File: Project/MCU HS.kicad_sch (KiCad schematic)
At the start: 21 parts, among them J2 SM04B, U1 STM32F072CBUx, U3 XC6206PxxxMR, U4 PRTR5V0U2X

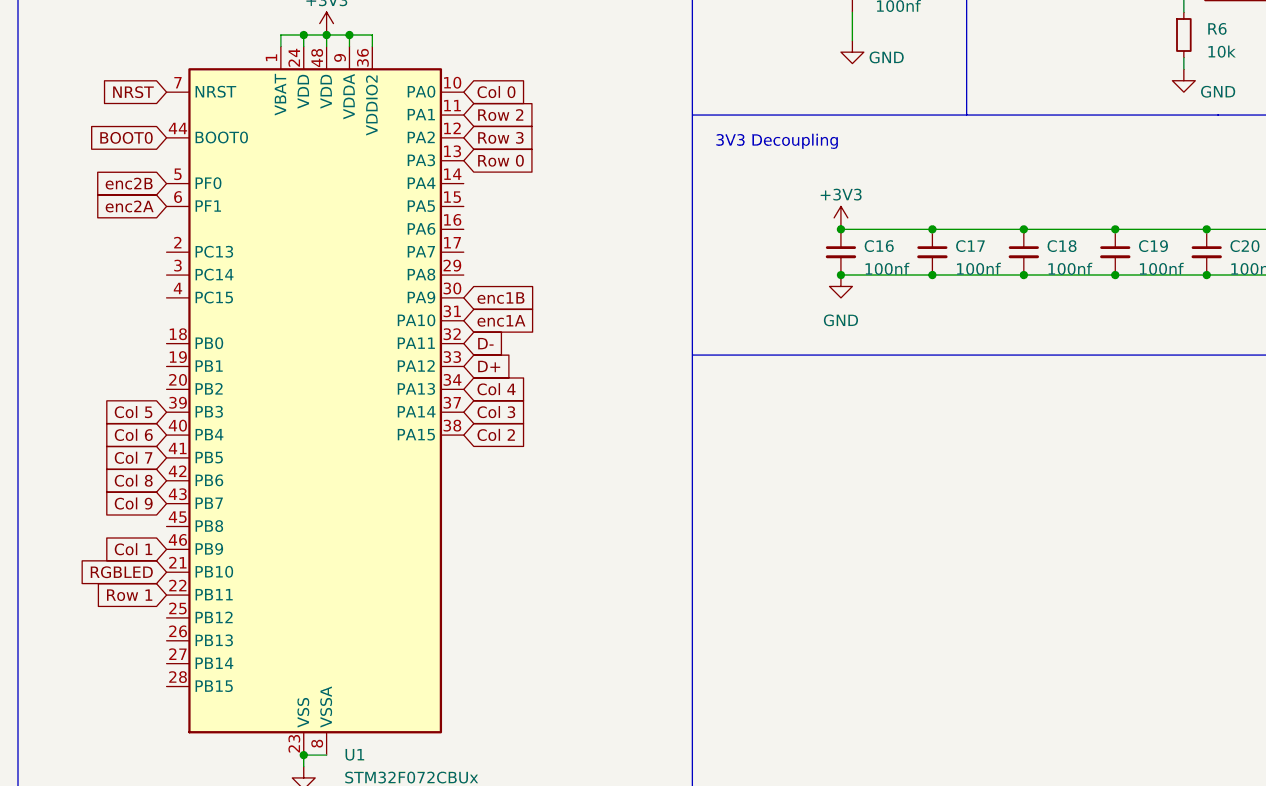
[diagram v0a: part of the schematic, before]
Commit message: 6 MCU pin breakouts added, readded silkscreen, fresh production files
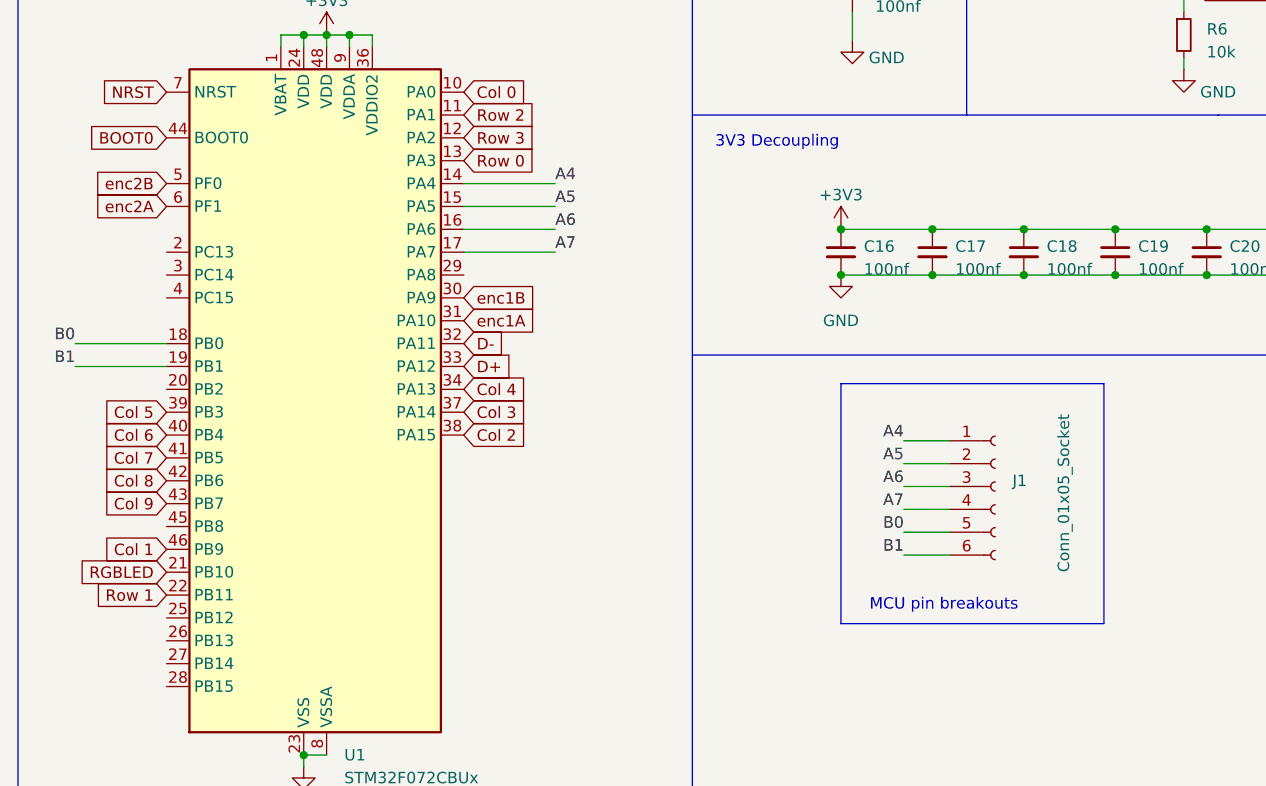
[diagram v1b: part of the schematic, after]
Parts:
- added J1: Conn_01x05_Socket, Connector_PinHeader_2.00mm:PinHeader_1x06_P2.00mm_Vertical, symbol Connector:Conn_01x06_Socket
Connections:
- net A4: now reaches U1.14 (PA4)
- net A4: now also J1.1 (Pin_1)
- net A5: now reaches U1.15 (PA5)
- net A5: now also J1.2 (Pin_2)
- net A6: now reaches U1.16 (PA6)
- net A6: now also J1.3 (Pin_3)
- net A7: now reaches U1.17 (PA7)
- net A7: now also J1.4 (Pin_4)
- net B0: now reaches U1.18 (PB0)
- net B0: now also J1.5 (Pin_5)
- net B1: now reaches U1.19 (PB1)
- net B1: now also J1.6 (Pin_6)
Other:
- note added: "MCU pin breakouts"
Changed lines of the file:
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@@
+    (stroke (width 0) (type default))
+  )
+  (wire (pts (xy 68.58 49.53) (xy 78.74 49.53))
     (stroke (width 0) (type default))
   )
@@
     (stroke (width 0) (type default))
   )
+  (wire (pts (xy 117.475 85.725) (xy 122.555 85.725))
+    (stroke (width 0) (type default))
+  )
   (wire (pts (xy 50.8 113.03) (xy 53.34 113.03))
     (stroke (width 0) (type default))
@@
     (stroke (width 0) (type default))
   )
+  (wire (pts (xy 117.475 78.105) (xy 122.555 78.105))
+    (stroke (width 0) (type default))
+  )
   (wire (pts (xy 262.89 52.07) (xy 264.795 52.07))
     (stroke (width 0) (type default))
@@
     (stroke (width 0) (type default))
   )
+  (wire (pts (xy 117.475 90.805) (xy 122.555 90.805))
+    (stroke (width 0) (type default))
+  )
   (polyline (pts (xy 93.98 68.58) (xy 171.45 68.58))
     (stroke (width 0) (type default))
@@
     (stroke (width 0) (type default))
   )
+  (wire (pts (xy 35.56 67.31) (xy 25.4 67.31))
+    (stroke (width 0) (type default))
+  )
   (wire (pts (xy 148.59 27.94) (xy 148.59 30.48))
     (stroke (width 0) (type default))
@@
     (stroke (width 0) (type default))
   )
+  (wire (pts (xy 68.58 57.15) (xy 78.74 57.15))
+    (stroke (width 0) (type default))
+  )
   (wire (pts (xy 224.155 76.835) (xy 224.155 84.455))
     (stroke (width 0) (type default))
@@
     (stroke (width 0) (type default))
   )
+  (wire (pts (xy 117.475 88.265) (xy 122.555 88.265))
+    (stroke (width 0) (type default))
+  )
   (wire (pts (xy 231.14 31.75) (xy 240.665 31.75))
     (stroke (width 0) (type default))
@@
     (stroke (width 0) (type default))
   )
+  (wire (pts (xy 68.58 52.07) (xy 78.74 52.07))
+    (stroke (width 0) (type default))
+  )
+  (wire (pts (xy 68.58 54.61) (xy 78.74 54.61))
+    (stroke (width 0) (type default))
+  )
   (polyline (pts (xy 278.13 66.04) (xy 208.28 66.04))
     (stroke (width 0) (type default))
@@
     (stroke (width 0) (type default))
   )
+  (wire (pts (xy 35.56 69.85) (xy 25.4 69.85))
+    (stroke (width 0) (type default))
+  )
   (wire (pts (xy 270.51 78.74) (xy 270.51 80.645))
     (stroke (width 0) (type default))
   )
+  (wire (pts (xy 117.475 80.645) (xy 122.555 80.645))
+    (stroke (width 0) (type default))
+  )
+  (wire (pts (xy 117.475 83.185) (xy 122.555 83.185))
+    (stroke (width 0) (type default))
+  )
   (wire (pts (xy 226.695 101.6) (xy 234.95 101.6))
     (stroke (width 0) (type default))
@@
     (stroke (width 0) (type default))
   )
+  (rectangle (start 110.49 71.755) (end 139.7 98.425)
+    (stroke (width 0) (type default))
+    (fill (type none))
+  )
   (text "Power Regulation" (at 209.55 95.25 0)
     (effects (font (size 1.27 1.27)) (justify left bottom))
@@
   )
   (text "3V3 Decoupling" (at 96.52 45.72 0)
+    (effects (font (size 1.27 1.27)) (justify left bottom))
+  )
+  (text "MCU pin breakouts" (at 113.665 97.155 0)
+    (effects (font (size 1.27 1.27)) (justify left bottom))
+  )
+  (label "A4" (at 117.475 78.105 180) (fields_autoplaced)
+    (effects (font (size 1.27 1.27)) (justify right bottom))
+  )
+  (label "A7" (at 117.475 85.725 180) (fields_autoplaced)
+    (effects (font (size 1.27 1.27)) (justify right bottom))
+  )
+  (label "B1" (at 117.475 90.805 180) (fields_autoplaced)
+    (effects (font (size 1.27 1.27)) (justify right bottom))
+  )
+  (label "A6" (at 117.475 83.185 180) (fields_autoplaced)
+    (effects (font (size 1.27 1.27)) (justify right bottom))
+  )
+  (label "B0" (at 25.4 67.31 180) (fields_autoplaced)
+    (effects (font (size 1.27 1.27)) (justify right bottom))
+  )
+  (label "A6" (at 78.74 54.61 0) (fields_autoplaced)
+    (effects (font (size 1.27 1.27)) (justify left bottom))
+  )
+  (label "B0" (at 117.475 88.265 180) (fields_autoplaced)
+    (effects (font (size 1.27 1.27)) (justify right bottom))
+  )
+  (label "A4" (at 78.74 49.53 0) (fields_autoplaced)
+    (effects (font (size 1.27 1.27)) (justify left bottom))
+  )
+  (label "B1" (at 25.4 69.85 180) (fields_autoplaced)
+    (effects (font (size 1.27 1.27)) (justify right bottom))
+  )
+  (label "A7" (at 78.74 57.15 0) (fields_autoplaced)
+    (effects (font (size 1.27 1.27)) (justify left bottom))
+  )
+  (label "A5" (at 117.475 80.645 180) (fields_autoplaced)
+    (effects (font (size 1.27 1.27)) (justify right bottom))
+  )
+  (label "A5" (at 78.74 52.07 0) (fields_autoplaced)
     (effects (font (size 1.27 1.27)) (justify left bottom))
   )
@@
         )
       )
+    )
+  )
+  (symbol (lib_id "Connector:Conn_01x06_Socket") (at 127.635 83.185 0) (unit 1)
+    (in_bom yes) (on_board yes) (dnp no)
+    (property "Reference" "J1" (at 129.54 82.55 0)
+      (effects (font (size 1.27 1.27)) (justify left))
+    )
+    (property "Value" "Conn_01x05_Socket" (at 135.255 92.71 90)
+      (effects (font (size 1.27 1.27)) (justify left))
+    )
+    (property "Footprint" "Connector_PinHeader_2.00mm:PinHeader_1x06_P2.00mm_Vertical" (at 127.635 83.185 0)
+      (effects (font (size 1.27 1.27)) hide)
+    )
+    (property "Datasheet" "~" (at 127.635 83.185 0)
+      (effects (font (size 1.27 1.27)) hide)
+    )
+    (pin "1")
+    (pin "2")
+    (pin "3")
+    (pin "4")
+    (pin "5")
+    (pin "6")
+    (instances
+      (project "Infernum HS"
+        (path "/e63e39d7-6ac0-4ffd-8aa3-1841a4541b55/d0969589-facd-430d-a52b-74c4e073ccb0"
+          (reference "J1") (unit 1)
+        )
+      )

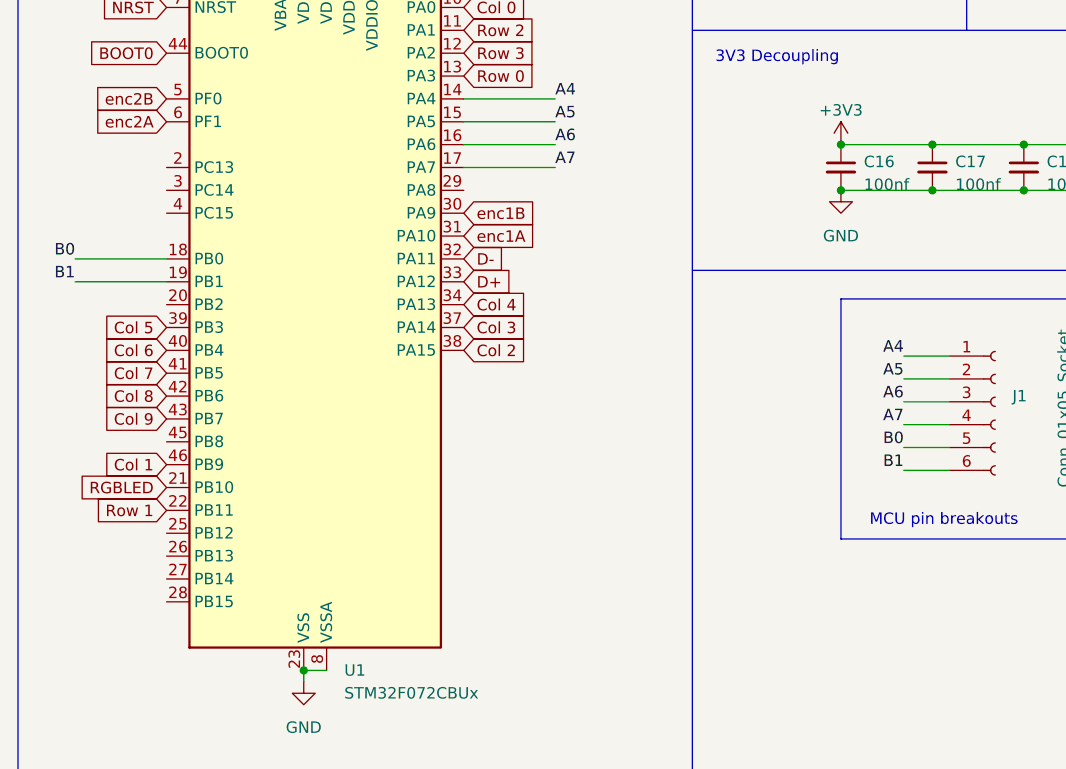
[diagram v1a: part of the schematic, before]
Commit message: changed pinout for pimoroni support, fresh gerbers
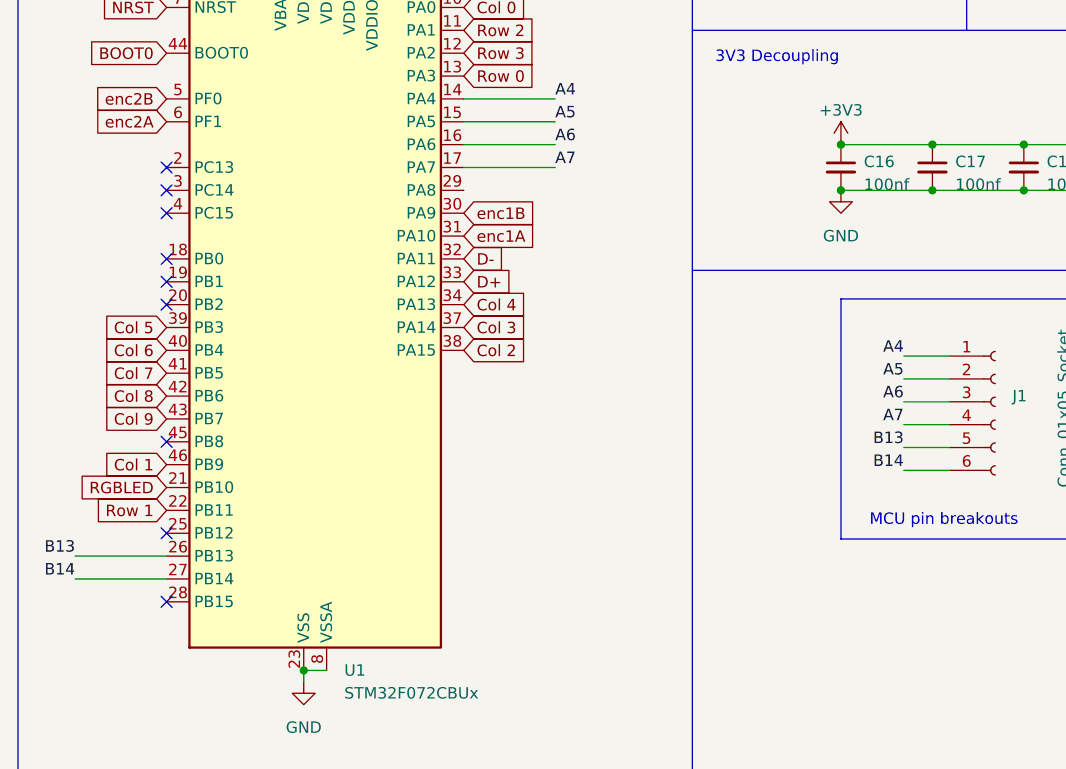
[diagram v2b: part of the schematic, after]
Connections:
- net B13: now reaches U1.26 (PB13)
- net B13: now also J1.5 (Pin_5)
- net B14: now reaches U1.27 (PB14)
- net B14: now also J1.6 (Pin_6)
- net B0: no longer names the net of U1.18 (PB0)
- net B0: no longer J1.5 (Pin_5)
- net B1: no longer names the net of U1.19 (PB1)
- net B1: no longer J1.6 (Pin_6)
- no-connect marks 2 -> 11
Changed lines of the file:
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@@
   (junction (at 140.97 59.69) (diameter 0) (color 0 0 0 0)
   )
+  (no_connect (at 35.56 87.63))
+  (no_connect (at 35.56 67.31))
+  (no_connect (at 35.56 105.41))
+  (no_connect (at 35.56 69.85))
+  (no_connect (at 35.56 72.39))
   (no_connect (at 231.14 34.29))
+  (no_connect (at 35.56 62.23))
+  (no_connect (at 35.56 97.79))
+  (no_connect (at 35.56 57.15))
   (no_connect (at 231.14 49.53))
+  (no_connect (at 35.56 59.69))
   (wire (pts (xy 50.8 114.3) (xy 50.8 113.03))
     (stroke (width 0) (type default))
@@
     (stroke (width 0) (type default))
   )
-  (wire (pts (xy 35.56 67.31) (xy 25.4 67.31))
-    (stroke (width 0) (type default))
-  )
   (wire (pts (xy 148.59 27.94) (xy 148.59 30.48))
     (stroke (width 0) (type default))
@@
     (stroke (width 0) (type default))
   )
+  (wire (pts (xy 35.56 102.87) (xy 25.4 102.87))
+    (stroke (width 0) (type default))
+  )
+  (wire (pts (xy 35.56 100.33) (xy 25.4 100.33))
+    (stroke (width 0) (type default))
+  )
   (wire (pts (xy 68.58 54.61) (xy 78.74 54.61))
     (stroke (width 0) (type default))
@@
     (stroke (width 0) (type default))
   )
-  (wire (pts (xy 35.56 69.85) (xy 25.4 69.85))
-    (stroke (width 0) (type default))
-  )
   (wire (pts (xy 270.51 78.74) (xy 270.51 80.645))
     (stroke (width 0) (type default))
@@
     (effects (font (size 1.27 1.27)) (justify right bottom))
   )
-  (label "B1" (at 117.475 90.805 180) (fields_autoplaced)
+  (label "B14" (at 117.475 90.805 180) (fields_autoplaced)
+    (effects (font (size 1.27 1.27)) (justify right bottom))
+  )
+  (label "B13" (at 25.4 100.33 180) (fields_autoplaced)
     (effects (font (size 1.27 1.27)) (justify right bottom))
   )
@@
     (effects (font (size 1.27 1.27)) (justify right bottom))
   )
-  (label "B0" (at 25.4 67.31 180) (fields_autoplaced)
+  (label "B14" (at 25.4 102.87 180) (fields_autoplaced)
     (effects (font (size 1.27 1.27)) (justify right bottom))
   )
@@
     (effects (font (size 1.27 1.27)) (justify left bottom))
   )
-  (label "B0" (at 117.475 88.265 180) (fields_autoplaced)
+  (label "B13" (at 117.475 88.265 180) (fields_autoplaced)
     (effects (font (size 1.27 1.27)) (justify right bottom))
   )
@@
     (effects (font (size 1.27 1.27)) (justify left bottom))
   )
-  (label "B1" (at 25.4 69.85 180) (fields_autoplaced)
-    (effects (font (size 1.27 1.27)) (justify right bottom))
-  )
   (label "A7" (at 78.74 57.15 0) (fields_autoplaced)

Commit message: fresh production
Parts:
- added J4: Conn_01x03_Socket, Connector_PinHeader_2.00mm:PinHeader_1x03_P2.00mm_Vertical, symbol Connector:Conn_01x03_Socket
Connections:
- net +3V3: now also J4.2 (Pin_2)
- net +5V: now also J4.3 (Pin_3)
- net GND: now also J4.1 (Pin_1)
- no-connect marks 11 -> 12
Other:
- note added: "Power Breakout"
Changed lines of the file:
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@@
   (no_connect (at 35.56 57.15))
   (no_connect (at 231.14 49.53))
+  (no_connect (at 68.58 59.69))
   (no_connect (at 35.56 59.69))
   (wire (pts (xy 50.8 114.3) (xy 50.8 113.03))
@@
     (stroke (width 0) (type default))
   )
+  (rectangle (start 144.145 71.755) (end 170.815 98.425)
+    (stroke (width 0) (type default))
+    (fill (type none))
+  )
   (rectangle (start 110.49 71.755) (end 139.7 98.425)
     (stroke (width 0) (type default))
@@
   )
   (text "3V3 Decoupling" (at 96.52 45.72 0)
+    (effects (font (size 1.27 1.27)) (justify left bottom))
+  )
+  (text "Power Breakout" (at 144.78 97.155 0)
     (effects (font (size 1.27 1.27)) (justify left bottom))
   )
@@
     )
   )
+  (symbol (lib_id "power:GND") (at 153.035 82.55 270) (unit 1)
+    (in_bom yes) (on_board yes) (dnp no)
+    (property "Reference" "#PWR010" (at 146.685 82.55 0)
+      (effects (font (size 1.27 1.27)) hide)
+    )
+    (property "Value" "GND" (at 149.225 82.55 90)
+      (effects (font (size 1.27 1.27)) (justify right))
+    )
+    (property "Footprint" "" (at 153.035 82.55 0)
+      (effects (font (size 1.27 1.27)) hide)
+    )
+    (property "Datasheet" "" (at 153.035 82.55 0)
+      (effects (font (size 1.27 1.27)) hide)
+    )
+    (pin "1")
+    (instances
+      (project "Infernum HS"
+        (path "/e63e39d7-6ac0-4ffd-8aa3-1841a4541b55/d0969589-facd-430d-a52b-74c4e073ccb0"
+          (reference "#PWR010") (unit 1)
+        )
+      )
+    )
+  )
   (symbol (lib_id "Device:C_Small") (at 226.695 105.41 0) (unit 1)
     (in_bom yes) (on_board yes) (dnp no) (fields_autoplaced)
@@
         (path "/e63e39d7-6ac0-4ffd-8aa3-1841a4541b55/d0969589-facd-430d-a52b-74c4e073ccb0"
           (reference "C_LDO2") (unit 1)
+        )
+      )
+    )
+  )
+  (symbol (lib_id "power:+3V3") (at 153.035 85.09 90) (mirror x) (unit 1)
+    (in_bom yes) (on_board yes) (dnp no)
+    (property "Reference" "#PWR010" (at 156.845 85.09 0)
+      (effects (font (size 1.27 1.27)) hide)
+    )
+    (property "Value" "+3V3" (at 147.32 85.09 90)
+      (effects (font (size 1.27 1.27)))
+    )
+    (property "Footprint" "" (at 153.035 85.09 0)
+      (effects (font (size 1.27 1.27)) hide)
+    )
+    (property "Datasheet" "" (at 153.035 85.09 0)
+      (effects (font (size 1.27 1.27)) hide)
+    )
+    (pin "1")
+    (instances
+      (project "Eightu"
+        (path "/c4a24fcb-fcfe-47af-9a3c-3ffe86a38756"
+          (reference "#PWR010") (unit 1)
+        )
+      )
+      (project "stm32_hotswap_chiffre"
+        (path "/ca0d59d2-7f9b-4344-99bc-39bc2c8c88cb"
+          (reference "#PWR09") (unit 1)
+        )
+      )
+      (project "Infernum HS"
+        (path "/e63e39d7-6ac0-4ffd-8aa3-1841a4541b55/d0969589-facd-430d-a52b-74c4e073ccb0"
+          (reference "#PWR06") (unit 1)
         )
       )
@@
     )
   )
+  (symbol (lib_id "Connector:Conn_01x03_Socket") (at 158.115 85.09 0) (unit 1)
+    (in_bom yes) (on_board yes) (dnp no)
+    (property "Reference" "J4" (at 159.385 84.455 0)
+      (effects (font (size 1.27 1.27)) (justify left))
+    )
+    (property "Value" "Conn_01x03_Socket" (at 165.735 93.98 90)
+      (effects (font (size 1.27 1.27)) (justify left))
+    )
+    (property "Footprint" "Connector_PinHeader_2.00mm:PinHeader_1x03_P2.00mm_Vertical" (at 158.115 85.09 0)
+      (effects (font (size 1.27 1.27)) hide)
+    )
+    (property "Datasheet" "~" (at 158.115 85.09 0)
+      (effects (font (size 1.27 1.27)) hide)
+    )
+    (pin "1")
+    (pin "2")
+    (pin "3")
+    (instances
+      (project "Infernum HS"
+        (path "/e63e39d7-6ac0-4ffd-8aa3-1841a4541b55/d0969589-facd-430d-a52b-74c4e073ccb0"
+          (reference "J4") (unit 1)
+        )
+      )
+    )
+  )
   (symbol (lib_id "power:PWR_FLAG") (at 224.155 76.835 0) (unit 1)
     (in_bom yes) (on_board yes) (dnp no)
@@
         )
       )
+    )
+  )
+  (symbol (lib_id "power:+5V") (at 153.035 87.63 90) (unit 1)
+    (in_bom yes) (on_board yes) (dnp no)
+    (property "Reference" "#PWR07" (at 156.845 87.63 0)
+      (effects (font (size 1.27 1.27)) hide)
+    )
+    (property "Value" "+5V" (at 146.685 87.63 90)
+      (effects (font (size 1.27 1.27)))
+    )
+    (property "Footprint" "" (at 153.035 87.63 0)
+      (effects (font (size 1.27 1.27)) hide)
+    )
+    (property "Datasheet" "" (at 153.035 87.63 0)
+      (effects (font (size 1.27 1.27)) hide)
+    )
+    (pin "1")
+    (instances
+      (project "Infernum HS"
+        (path "/e63e39d7-6ac0-4ffd-8aa3-1841a4541b55/d0969589-facd-430d-a52b-74c4e073ccb0"
+          (reference "#PWR07") (unit 1)
+        )
+      )

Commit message: merged haizeus and my projects
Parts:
- removed J4: Conn_01x03_Socket, Connector_PinHeader_2.00mm:PinHeader_1x03_P2.00mm_Vertical, symbol Connector:Conn_01x03_Socket
- added J3: Conn_01x03_Socket, Connector_PinHeader_2.00mm:PinHeader_1x03_P2.00mm_Vertical, symbol Connector:Conn_01x03_Socket
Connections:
- net +3V3: now also J3.2 (Pin_2)
- net +5V: now also J3.3 (Pin_3)
- net GND: now also J3.1 (Pin_1)
- no-connect marks 12 -> 11
